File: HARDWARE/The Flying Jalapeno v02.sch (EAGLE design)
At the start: 100 parts, among them Q2 MMBT2222A, Q3 NDP6020P, Q4 MMBT2222A, Q5 NDP6020P, Q6 BSS138, 200mA/50V, Q7 BSS138, 200mA/50V, U1 ATMEGA2560AU, U2 LM1117, U3 LM1117, U4 LM1117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

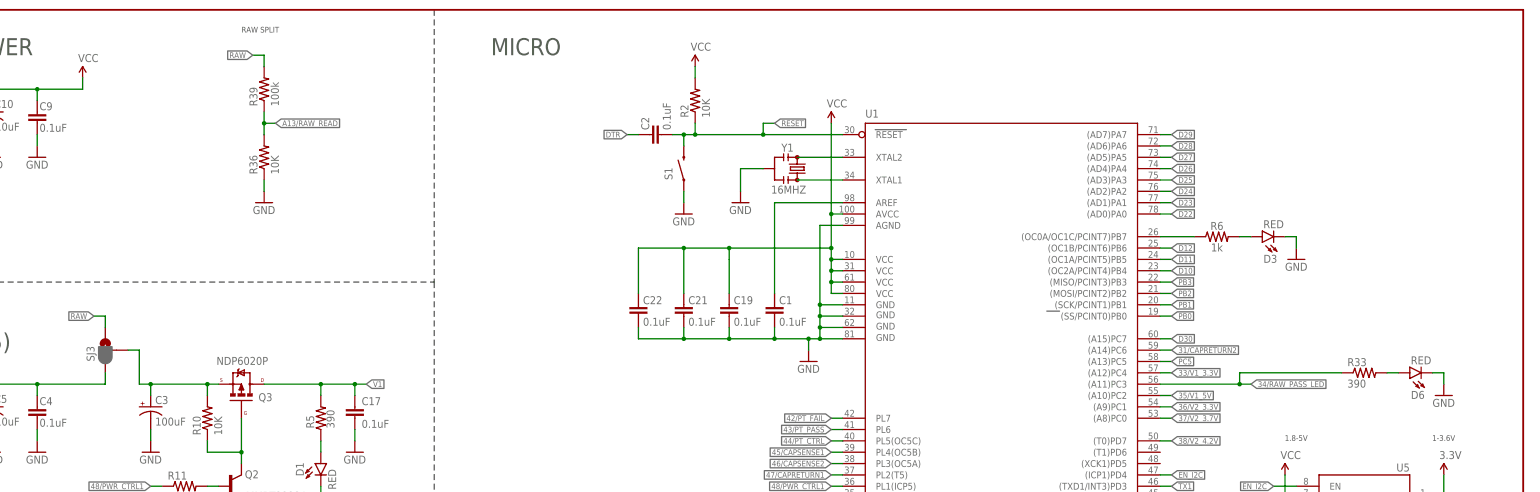
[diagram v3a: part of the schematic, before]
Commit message: removed RAW split test, moved pwr led from io to VCC
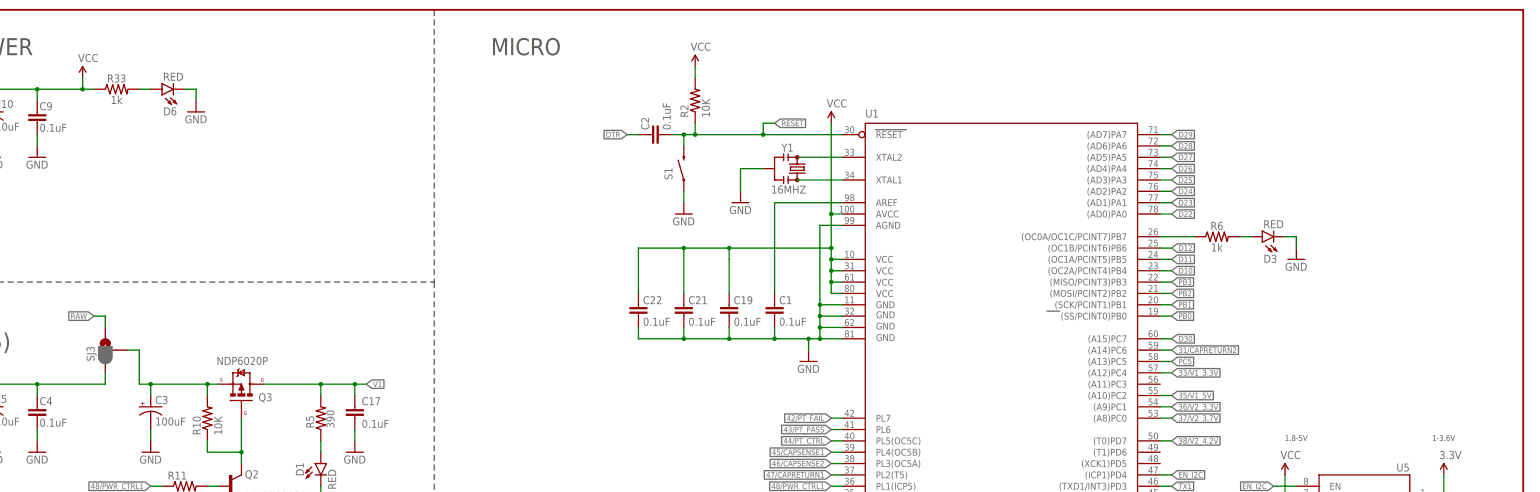
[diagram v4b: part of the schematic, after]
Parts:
- removed R36: 10K, SparkFun-Resistors:10KOHM-1/10W-1%(0603)0603
- removed R39: 100k, SparkFun-Resistors:100KOHM-1/10W-1%(0603)
- R33: value 390 -> 1k; device SparkFun-Resistors:390OHM1/10W1%(0603) -> SparkFun-Resistors:1KOHM-0603-1/10W-1%
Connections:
- removed net 34/RAW_PASS_LED: R33.1, U1.(A11)PC3
- net A13/RAW_READ: no longer R36.2, R39.1
- net GND: no longer R36.1
- net RAW: no longer R39.2
- net VCC: now also R33.1
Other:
- note removed: "RAW SPLIT"
- moved on the sheet: D6, R33
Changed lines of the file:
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@@
 <part name="STANDOFF3" library="SparkFun-Electromechanical" deviceset="STAND-OFF" device="TIGHT"/>
 <part name="STANDOFF4" library="SparkFun-Electromechanical" deviceset="STAND-OFF" device="TIGHT"/>
-<part name="R36" library="SparkFun-Resistors" deviceset="10KOHM-1/10W-1%(0603)" device="0603" value="10K"/>
-<part name="GND38" library="SparkFun" deviceset="GND" device=""/>
 <part name="R37" library="SparkFun-Resistors" deviceset="100OHM-1/10W-1%(0603)" device="" value="100"/>
 <part name="R38" library="SparkFun-Resistors" deviceset="470OHM1/10W1%(0603)" device="" value="470"/>
-<part name="R39" library="SparkFun-Resistors" deviceset="100KOHM-1/10W-1%(0603)" device="" value="100k"/>
 <part name="C19" library="SparkFun-Capacitors" deviceset="0.1UF-25V(+80/-20%)(0603)" device="" value="0.1uF"/>
 <part name="C21" library="SparkFun-Capacitors" deviceset="0.1UF-25V(+80/-20%)(0603)" device="" value="0.1uF"/>
@@
 <part name="D6" library="SparkFun-LED" deviceset="LED-RED" device="1206" value="RED"/>
 <part name="GND5" library="SparkFun" deviceset="GND" device=""/>
-<part name="R33" library="SparkFun-Resistors" deviceset="390OHM1/10W1%(0603)" device="" value="390"/>
+<part name="R33" library="SparkFun-Resistors" deviceset="1KOHM" device="-0603-1/10W-1%" value="1k"/>
 <part name="Q6" library="SparkFun-DiscreteSemi" deviceset="MOSFET-NCHANNEL" device="BSS138" value="BSS138, 200mA/50V"/>
 <part name="P+1" library="SparkFun" deviceset="VCC" device="" value="FTDI_VCC"/>
@@
 <text x="354.33" y="11.43" size="2.54" layer="94">Pete Lewis</text>
 <text x="422.402" y="7.62" size="2.54" layer="94">v02</text>
-<text x="144.78" y="274.32" size="1.27" layer="97">RAW SPLIT</text>
 <text x="284.48" y="96.52" size="1.778" layer="97">ATMEGA2560V</text>
 <text x="457.2" y="246.38" size="3.81" layer="97">2x30 RA connector to testbeds</text>
@@
 <instance part="STANDOFF3" gate="G$1" x="429.26" y="27.94"/>
 <instance part="STANDOFF4" gate="G$1" x="426.72" y="27.94"/>
-<instance part="R36" gate="G$1" x="149.86" y="246.38" rot="R90"/>
-<instance part="GND38" gate="1" x="149.86" y="236.22"/>
 <instance part="R37" gate="G$1" x="88.9" y="96.52" rot="R180"/>
 <instance part="R38" gate="G$1" x="83.82" y="109.22" rot="R90"/>
 <instance part="GND47" gate="1" x="22.86" y="22.86"/>
 <instance part="JP2" gate="G$1" x="15.24" y="35.56" rot="MR180"/>
-<instance part="R39" gate="G$1" x="149.86" y="261.62" rot="R90"/>
 <instance part="U1" gate="1" x="314.96" y="175.26" smashed="yes">
 <attribute name="NAME" x="284.48" y="255.27" size="1.778" layer="95"/>
@@
 <attribute name="VALUE" x="541.17" y="161.458" size="0.8128" layer="96"/>
 </instance>
-<instance part="D6" gate="G$1" x="406.4" y="198.12" smashed="yes" rot="R90">
-<attribute name="NAME" x="406.654" y="192.278" size="1.778" layer="95"/>
-<attribute name="VALUE" x="411.226" y="201.803" size="1.778" layer="96" rot="R180"/>
-</instance>
-<instance part="GND5" gate="1" x="414.02" y="193.04"/>
-<instance part="R33" gate="G$1" x="396.24" y="198.12"/>
+<instance part="D6" gate="G$1" x="127" y="261.62" smashed="yes" rot="R90">
+<attribute name="NAME" x="127.254" y="255.778" size="1.778" layer="95"/>
+<attribute name="VALUE" x="131.826" y="265.303" size="1.778" layer="96" rot="R180"/>
+</instance>
+<instance part="GND5" gate="1" x="134.62" y="256.54"/>
+<instance part="R33" gate="G$1" x="116.84" y="261.62"/>
 <instance part="Q6" gate="G$1" x="45.72" y="38.1" smashed="yes" rot="R270">
 <attribute name="NAME" x="41.91" y="42.926" size="1.778" layer="95"/>
@@
 <pinref part="C18" gate="G$1" pin="2"/>
 <wire x1="175.26" y1="119.38" x2="175.26" y2="121.92" width="0.1524" layer="91"/>
-</segment>
-<segment>
-<pinref part="R36" gate="G$1" pin="1"/>
-<pinref part="GND38" gate="1" pin="GND"/>
-<wire x1="149.86" y1="238.76" x2="149.86" y2="241.3" width="0.1524" layer="91"/>
 </segment>
 <segment>
@@
 <segment>
 <pinref part="GND5" gate="1" pin="GND"/>
-<wire x1="414.02" y1="195.58" x2="414.02" y2="198.12" width="0.1524" layer="91"/>
+<wire x1="134.62" y1="259.08" x2="134.62" y2="261.62" width="0.1524" layer="91"/>
 <pinref part="D6" gate="G$1" pin="C"/>
-<wire x1="414.02" y1="198.12" x2="411.48" y2="198.12" width="0.1524" layer="91"/>
+<wire x1="134.62" y1="261.62" x2="132.08" y2="261.62" width="0.1524" layer="91"/>
 </segment>
 <segment>
@@
 <wire x1="78.74" y1="259.08" x2="78.74" y2="261.62" width="0.1524" layer="91"/>
 <junction x="78.74" y="261.62"/>
+<pinref part="R33" gate="G$1" pin="1"/>
+<wire x1="109.22" y1="261.62" x2="111.76" y2="261.62" width="0.1524" layer="91"/>
+<junction x="109.22" y="261.62"/>
 </segment>
 <segment>
@@
 </segment>
 <segment>
-<wire x1="149.86" y1="266.7" x2="149.86" y2="269.24" width="0.1524" layer="91"/>
-<wire x1="149.86" y1="269.24" x2="147.32" y2="269.24" width="0.1524" layer="91"/>
-<label x="147.32" y="269.24" size="1.27" layer="95" rot="R180" xref="yes"/>
-<pinref part="R39" gate="G$1" pin="2"/>
-</segment>
-<segment>
 <pinref part="JP4" gate="G$1" pin="RAW"/>
 <wire x1="480.06" y1="231.14" x2="477.52" y2="231.14" width="0.1524" layer="91"/>
@@
 <net name="A13/RAW_READ" class="0">
 <segment>
-<pinref part="R36" gate="G$1" pin="2"/>
-<wire x1="149.86" y1="251.46" x2="149.86" y2="254" width="0.1524" layer="91"/>
-<wire x1="149.86" y1="254" x2="149.86" y2="256.54" width="0.1524" layer="91"/>
-<wire x1="149.86" y1="254" x2="152.4" y2="254" width="0.1524" layer="91"/>
-<junction x="149.86" y="254"/>
-<label x="152.4" y="254" size="1.27" layer="95" xref="yes"/>
-<pinref part="R39" gate="G$1" pin="1"/>
-</segment>
-<segment>
 <wire x1="279.4" y1="160.02" x2="276.86" y2="160.02" width="0.1524" layer="91"/>
 <pinref part="U1" gate="1" pin="PK5(ADC13/PCINT21)"/>
@@
 </segment>
 </net>
-<net name="34/RAW_PASS_LED" class="0">
-<segment>
-<wire x1="350.52" y1="195.58" x2="368.3" y2="195.58" width="0.1524" layer="91"/>
-<pinref part="U1" gate="1" pin="(A11)PC3"/>
-<label x="370.84" y="195.58" size="1.27" layer="95" xref="yes"/>
-<wire x1="368.3" y1="195.58" x2="370.84" y2="195.58" width="0.1524" layer="91"/>
-<wire x1="368.3" y1="195.58" x2="368.3" y2="198.12" width="0.1524" layer="91"/>
-<junction x="368.3" y="195.58"/>
-<pinref part="R33" gate="G$1" pin="1"/>
-<wire x1="368.3" y1="198.12" x2="391.16" y2="198.12" width="0.1524" layer="91"/>
-</segment>
-</net>
 <net name="PC5" class="0">
 <segment>
@@
 <pinref part="D6" gate="G$1" pin="A"/>
 <pinref part="R33" gate="G$1" pin="2"/>
-<wire x1="401.32" y1="198.12" x2="403.86" y2="198.12" width="0.1524" layer="91"/>
-</segment>
-</net>
+<wire x1="121.92" y1="261.62" x2="124.46" y2="261.62" width="0.1524" layer="91"/>
+</segment>
+</net>

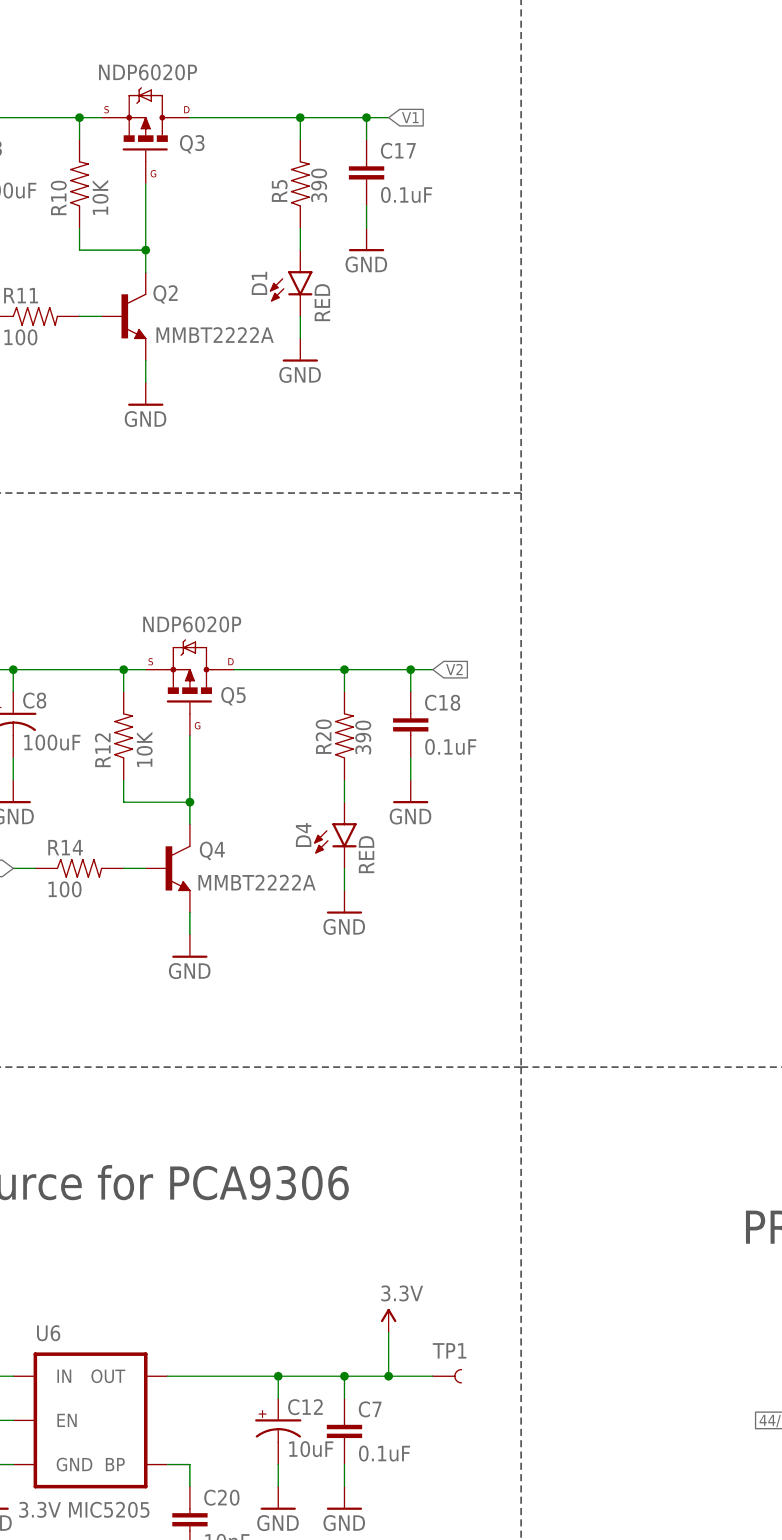
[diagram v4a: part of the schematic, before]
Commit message: moved V1 and V2 leds resistors to 1K
also update silk labeling
also removed test point on 3.3V vreg output
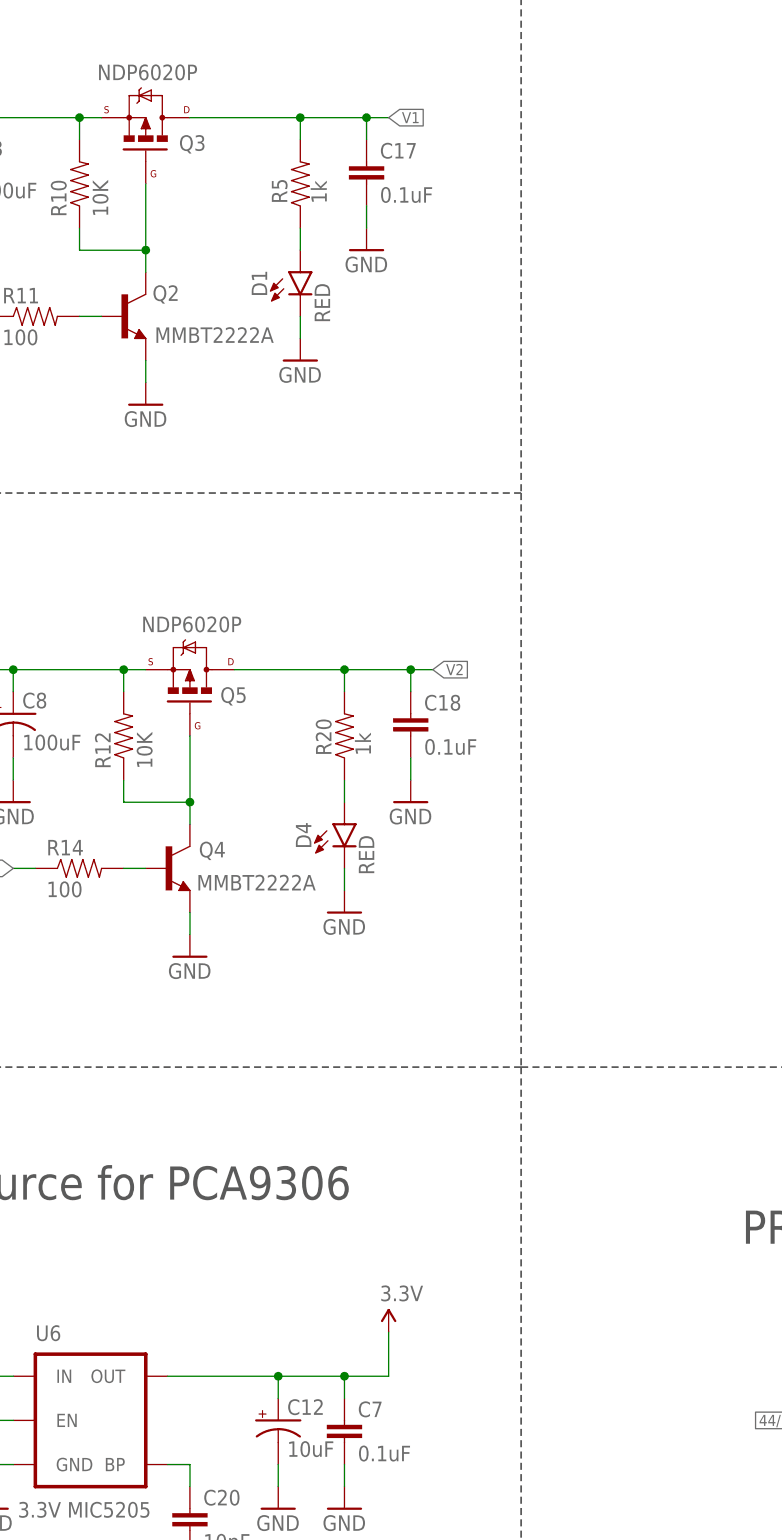
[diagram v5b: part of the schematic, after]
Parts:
- removed TP1: TEST-POINT3, SparkFun-Passives:TEST-POINT3
- R20, R5: value 390 -> 1k; device SparkFun-Resistors:390OHM1/10W1%(0603) -> SparkFun-Resistors:1KOHM-0603-1/10W-1%
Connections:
- net 3.3V: no longer TP1.1
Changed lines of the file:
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@@
 <part name="D1" library="SparkFun-LED" deviceset="LED-RED" device="1206" value="RED"/>
 <part name="GND10" library="SparkFun" deviceset="GND" device=""/>
-<part name="R5" library="SparkFun-Resistors" deviceset="390OHM1/10W1%(0603)" device="" value="390"/>
+<part name="R5" library="SparkFun-Resistors" deviceset="1KOHM" device="-0603-1/10W-1%" value="1k"/>
 <part name="R7" library="SparkFun-Resistors" deviceset="390OHM1/10W1%(0603)" device="" value="390"/>
 <part name="C13" library="SparkFun-Capacitors" deviceset="0.1UF-25V(+80/-20%)(0603)" device="" value="0.1uF"/>
@@
 <part name="D4" library="SparkFun-LED" deviceset="LED-RED" device="1206" value="RED"/>
 <part name="GND31" library="SparkFun" deviceset="GND" device=""/>
-<part name="R20" library="SparkFun-Resistors" deviceset="390OHM1/10W1%(0603)" device="" value="390"/>
+<part name="R20" library="SparkFun-Resistors" deviceset="1KOHM" device="-0603-1/10W-1%" value="1k"/>
 <part name="R21" library="SparkFun-Resistors" deviceset="715OHM1/10W1%(0603)" device="" value="715"/>
 <part name="SJ3" library="SparkFun-Passives" deviceset="JUMPER-PAD-3-2OF3_NC_BY_PASTE" device="" value=""/>
@@
 <part name="GND12" library="SparkFun" deviceset="GND" device=""/>
 <part name="P+12" library="SparkFun" deviceset="3.3V" device=""/>
-<part name="TP1" library="SparkFun-Passives" deviceset="TEST-POINT" device="3"/>
 <part name="C12" library="SparkFun-Capacitors" deviceset="10UF-6.3V-20%(0603)(TANT)" device="&quot;" value="10uF"/>
 <part name="P+6" library="SparkFun" deviceset="3.3V" device="" value="VCC"/>
@@
 <instance part="GND12" gate="1" x="127" y="35.56"/>
 <instance part="P+12" gate="G$1" x="172.72" y="55.88"/>
-<instance part="TP1" gate="G$1" x="177.8" y="50.8" smashed="yes">
-<attribute name="NAME" x="177.8" y="52.832" size="1.778" layer="95"/>
-</instance>
 <instance part="C12" gate="G$1" x="160.02" y="45.72"/>
 <instance part="P+6" gate="G$1" x="378.46" y="175.26"/>
@@
 <pinref part="P+12" gate="G$1" pin="3.3V"/>
 <pinref part="C7" gate="G$1" pin="1"/>
-<pinref part="TP1" gate="G$1" pin="1"/>
-<wire x1="177.8" y1="50.8" x2="172.72" y2="50.8" width="0.1524" layer="91"/>
 <wire x1="172.72" y1="50.8" x2="167.64" y2="50.8" width="0.1524" layer="91"/>
 <wire x1="172.72" y1="55.88" x2="172.72" y2="50.8" width="0.1524" layer="91"/>
-<junction x="172.72" y="50.8"/>
 <pinref part="C12" gate="G$1" pin="+"/>
 </segment>
